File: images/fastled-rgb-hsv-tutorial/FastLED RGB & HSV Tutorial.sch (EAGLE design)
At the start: 13 parts

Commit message: Updated PCB
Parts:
- added A3: (no value), switch-omron:10-XX
- added R2: 10KΩ, SparkFun-Resistors:RESISTORPTH-1/4W-VERT-KIT
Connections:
- new net N$1: A3.S, R2.2
- new net S1: A3.S1, U$1.A3
- net 5V: now also A3.P
- net GND: now also R2.1
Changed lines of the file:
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@@
 <part name="LED3" library="SparkFun-Connectors" deviceset="M04" device="NO_SILK_ALL_ROUND"/>
 <part name="LED4" library="SparkFun-Connectors" deviceset="M04" device="NO_SILK_ALL_ROUND"/>
+<part name="A3" library="switch-omron" deviceset="10-XX" device=""/>
+<part name="R2" library="SparkFun-Resistors" deviceset="RESISTOR" device="PTH-1/4W-VERT-KIT" value="10KΩ"/>
 </parts>
 <sheets>
@@
 <instance part="LED3" gate="G$1" x="99.06" y="5.08"/>
 <instance part="LED4" gate="G$1" x="99.06" y="-15.24"/>
+<instance part="A3" gate="1" x="22.86" y="-15.24" rot="R90"/>
+<instance part="R2" gate="G$1" x="5.08" y="-15.24"/>
 </instances>
 <busses>
@@
 <label x="104.14" y="-30.48" size="1.778" layer="95"/>
 </segment>
+<segment>
+<pinref part="R2" gate="G$1" pin="1"/>
+<wire x1="0" y1="-15.24" x2="-5.08" y2="-15.24" width="0.1524" layer="91"/>
+<label x="-5.08" y="-15.24" size="1.778" layer="95"/>
+</segment>
 </net>
 <net name="5V" class="0">
@@
 <label x="104.14" y="-35.56" size="1.778" layer="95"/>
 </segment>
+<segment>
+<pinref part="A3" gate="1" pin="P"/>
+<wire x1="27.94" y1="-15.24" x2="33.02" y2="-15.24" width="0.1524" layer="91"/>
+<label x="30.48" y="-15.24" size="1.778" layer="95"/>
+</segment>
 </net>
 <net name="P0" class="0">
@@
 </segment>
 </net>
+<net name="N$1" class="0">
+<segment>
+<pinref part="A3" gate="1" pin="S"/>
+<pinref part="R2" gate="G$1" pin="2"/>
+<wire x1="17.78" y1="-15.24" x2="10.16" y2="-15.24" width="0.1524" layer="91"/>
+</segment>
+</net>
+<net name="S1" class="0">
+<segment>
+<pinref part="U$1" gate="G$1" pin="A3"/>
+<wire x1="0" y1="43.18" x2="-5.08" y2="43.18" width="0.1524" layer="91"/>
+<label x="-5.08" y="43.18" size="1.778" layer="95"/>
+</segment>
+<segment>
+<pinref part="A3" gate="1" pin="S1"/>
+<wire x1="17.78" y1="-12.7" x2="12.7" y2="-12.7" width="0.1524" layer="91"/>
+<label x="12.7" y="-12.7" size="1.778" layer="95"/>
+</segment>
+</net>

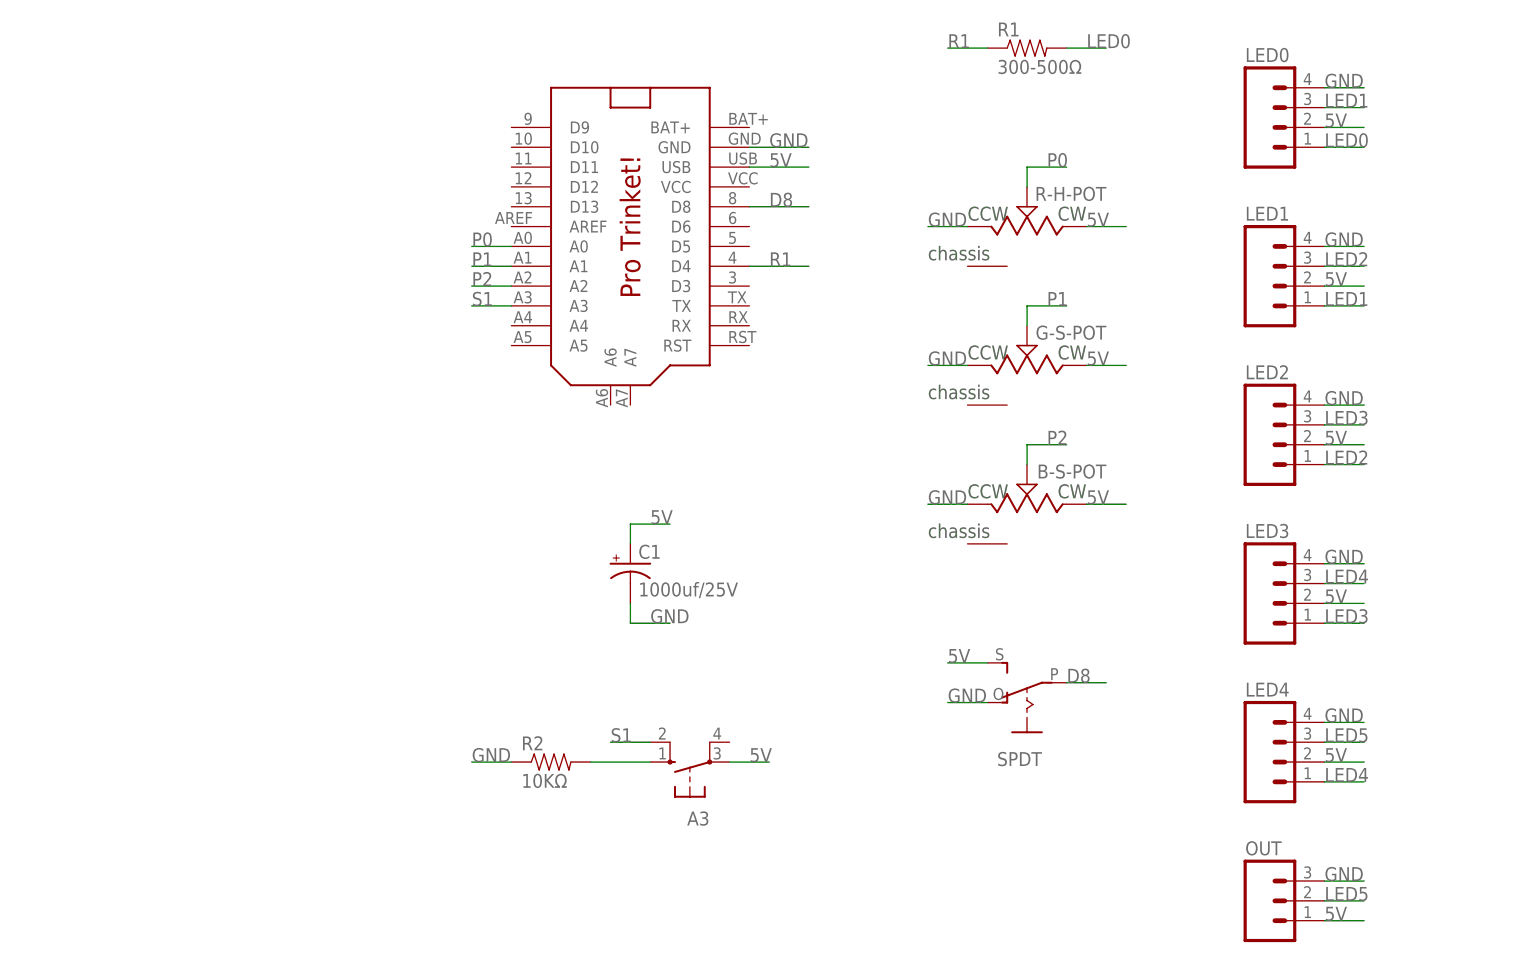
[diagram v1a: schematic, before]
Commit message: Switched to 8x NeoPixel stick.
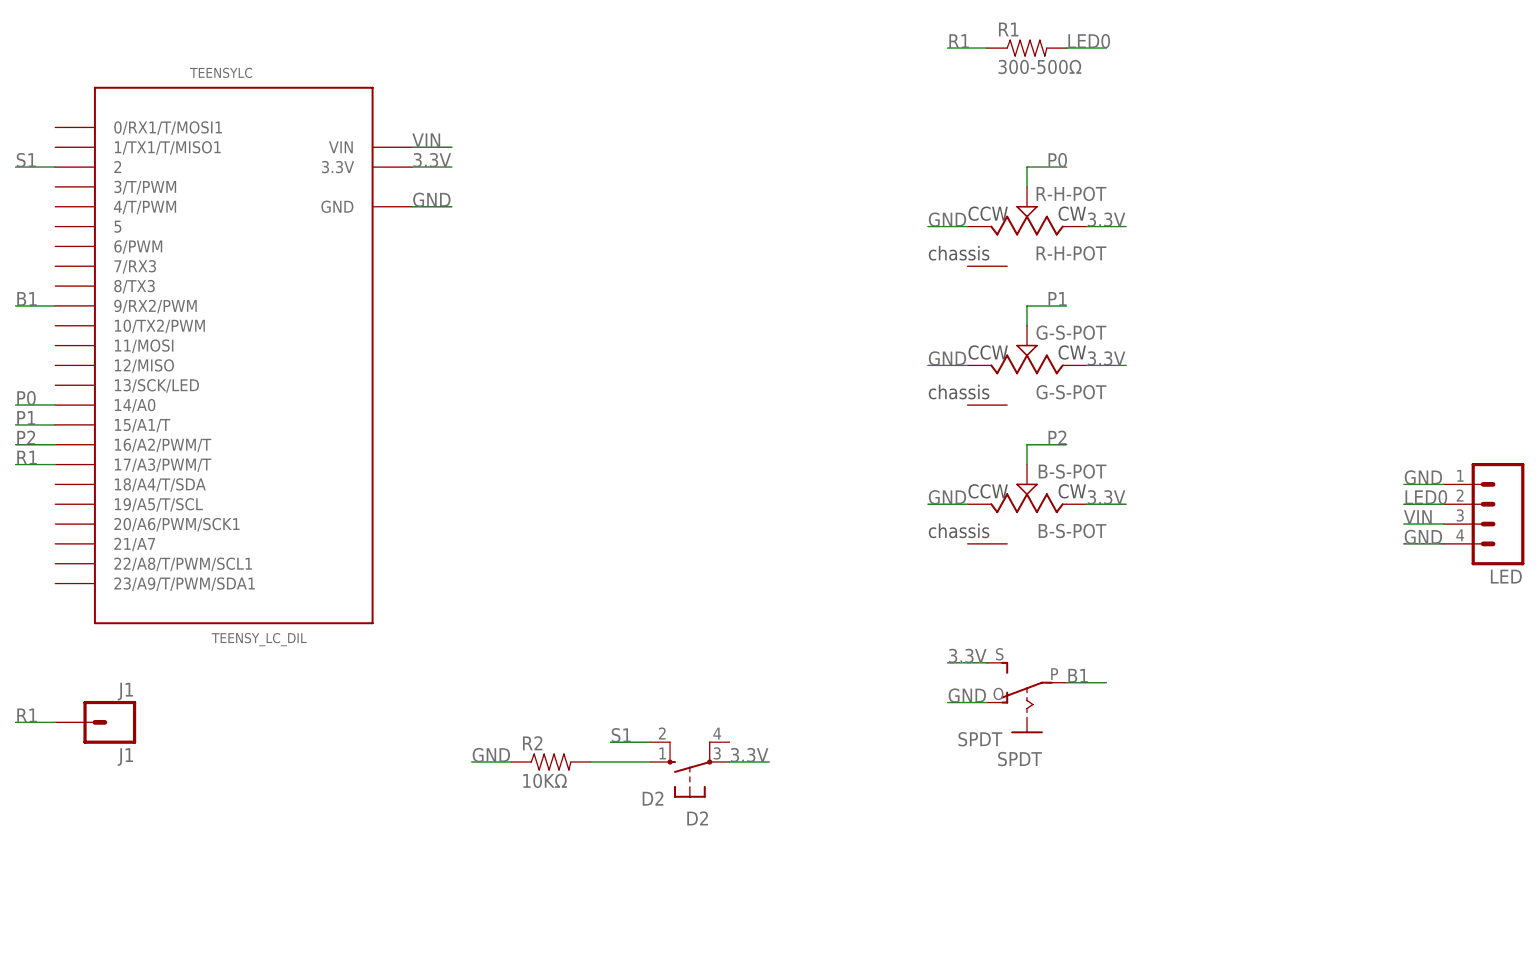
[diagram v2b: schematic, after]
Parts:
- removed C1: 1000uf/25V, SparkFun-Capacitors:1000UF-25V(PTH)KIT
- removed LED0, LED1, LED2, LED3, LED4: (no value), SparkFun-Connectors:M04NO_SILK_ALL_ROUND
- removed OUT: (no value), SparkFun-Connectors:M03PTH
- removed U$1: PRO_TRINKET, adafruit:PRO_TRINKET
- added J1: J1, SparkFun-Connectors:M01PTH
- added LED: (no value), SparkFun-Connectors:M04PTH
- added TEENSYLC: TEENSY_LC_DIL, Teensy_3_and_LC_Series_Boards_v1.1:TEENSY_LC_DIL
- B-S-POT: value (none) -> B-S-POT
- D2: value (none) -> D2
- G-S-POT: value (none) -> G-S-POT
- R-H-POT: value (none) -> R-H-POT
- SPDT: value (none) -> SPDT
- renumbered A3 to D2
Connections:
- removed net 5V: B-S-POT.CW, C1.+, D2.P, G-S-POT.CW, LED0.2, LED1.2, LED2.2, LED3.2, LED4.2, OUT.1, R-H-POT.CW, SPDT.S, U$1.USB
- removed net D8: SPDT.P, U$1.D8
- removed net LED1: LED0.3, LED1.1
- removed net LED2: LED1.3, LED2.1
- removed net LED3: LED2.3, LED3.1
- removed net LED4: LED3.3, LED4.1
- removed net LED5: LED4.3, OUT.2
- new net 3.3V: B-S-POT.CW, D2.P, G-S-POT.CW, R-H-POT.CW, SPDT.S, TEENSYLC.3.3V
- new net B1: SPDT.P, TEENSYLC.9/RX2/PWM
- new net VIN: LED.3, TEENSYLC.VIN
- net GND: now also LED.1, LED.4, TEENSYLC.GND; no longer C1.-, LED0.4, LED1.4, LED2.4, LED3.4, LED4.4, OUT.3, U$1.GND
- net LED0: now also LED.2; no longer LED0.1
- net P0: now also TEENSYLC.14/A0; no longer U$1.A0
- net P1: now also TEENSYLC.15/A1/T; no longer U$1.A1
- net P2: now also TEENSYLC.16/A2/PWM/T; no longer U$1.A2
- net R1: now also J1.1, TEENSYLC.17/A3/PWM/T; no longer U$1.D4
- net S1: now also TEENSYLC.2; no longer U$1.A3

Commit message: Added 10uF capacitor, reworked layout.
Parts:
- added C1: 10uF, SparkFun-Capacitors:10UF-25V-20%(PTH)KIT
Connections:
- net GND: now also C1.-
- net VIN: now also C1.+
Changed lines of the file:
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@@
 <part name="J1" library="SparkFun-Connectors" deviceset="M01" device="PTH" value="J1"/>
 <part name="LED" library="SparkFun-Connectors" deviceset="M04" device="PTH"/>
+<part name="C1" library="SparkFun-Capacitors" deviceset="10UF-25V-20%(PTH)" device="KIT" value="10uF"/>
 </parts>
 <sheets>
@@
 <instance part="J1" gate="G$1" x="-50.8" y="-10.16" rot="R180"/>
 <instance part="LED" gate="G$1" x="124.46" y="17.78" rot="R180"/>
+<instance part="C1" gate="G$1" x="17.78" y="30.48"/>
 </instances>
 <busses>
@@
 <wire x1="119.38" y1="12.7" x2="114.3" y2="12.7" width="0.1524" layer="91"/>
 <label x="114.3" y="12.7" size="1.778" layer="95"/>
+</segment>
+<segment>
+<pinref part="C1" gate="G$1" pin="-"/>
+<wire x1="17.78" y1="25.4" x2="17.78" y2="22.86" width="0.1524" layer="91"/>
+<wire x1="17.78" y1="22.86" x2="22.86" y2="22.86" width="0.1524" layer="91"/>
+<label x="17.78" y="22.86" size="1.778" layer="95"/>
 </segment>
 </net>
@@
 <label x="114.3" y="15.24" size="1.778" layer="95"/>
 </segment>
+<segment>
+<pinref part="C1" gate="G$1" pin="+"/>
+<wire x1="17.78" y1="33.02" x2="17.78" y2="35.56" width="0.1524" layer="91"/>
+<wire x1="17.78" y1="35.56" x2="22.86" y2="35.56" width="0.1524" layer="91"/>
+<label x="17.78" y="35.56" size="1.778" layer="95"/>
+</segment>
 </net>

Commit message: Updated site
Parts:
- removed J1: J1, SparkFun-Connectors:M01PTH
- added J6: (no value), SparkFun-Connectors:M05PTH
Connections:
- net GND: now also J6.3
- net R1: now also J6.1; no longer J1.1
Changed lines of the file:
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@@
 <part name="R2" library="SparkFun-Resistors" deviceset="RESISTOR" device="PTH-1/4W-VERT-KIT" value="10KΩ"/>
 <part name="TEENSYLC" library="Teensy_3_and_LC_Series_Boards_v1.1" deviceset="TEENSY_LC_DIL" device=""/>
-<part name="J1" library="SparkFun-Connectors" deviceset="M01" device="PTH" value="J1"/>
 <part name="LED" library="SparkFun-Connectors" deviceset="M04" device="PTH"/>
 <part name="C1" library="SparkFun-Capacitors" deviceset="10UF-25V-20%(PTH)" device="KIT" value="10uF"/>
+<part name="J6" library="SparkFun-Connectors" deviceset="M05" device="PTH"/>
 </parts>
 <sheets>
@@
 <instance part="R2" gate="G$1" x="5.08" y="-15.24"/>
 <instance part="TEENSYLC" gate="G$1" x="-35.56" y="35.56"/>
-<instance part="J1" gate="G$1" x="-50.8" y="-10.16" rot="R180"/>
 <instance part="LED" gate="G$1" x="124.46" y="17.78" rot="R180"/>
 <instance part="C1" gate="G$1" x="17.78" y="30.48"/>
+<instance part="J6" gate="G$1" x="-50.8" y="-15.24" rot="R180"/>
 </instances>
 <busses>
@@
 <wire x1="17.78" y1="22.86" x2="22.86" y2="22.86" width="0.1524" layer="91"/>
 <label x="17.78" y="22.86" size="1.778" layer="95"/>
+</segment>
+<segment>
+<pinref part="J6" gate="G$1" pin="3"/>
+<wire x1="-58.42" y1="-15.24" x2="-63.5" y2="-15.24" width="0.1524" layer="91"/>
+<label x="-63.5" y="-15.24" size="1.778" layer="95"/>
 </segment>
 </net>
@@
 </segment>
 <segment>
-<pinref part="J1" gate="G$1" pin="1"/>
 <wire x1="-58.42" y1="-10.16" x2="-63.5" y2="-10.16" width="0.1524" layer="91"/>
 <label x="-63.5" y="-10.16" size="1.778" layer="95"/>
+<pinref part="J6" gate="G$1" pin="1"/>
 </segment>
 <segment>
